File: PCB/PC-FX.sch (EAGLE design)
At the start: 11 parts, among them U1 SN74AHCT125N, U2 SN74AHCT125N

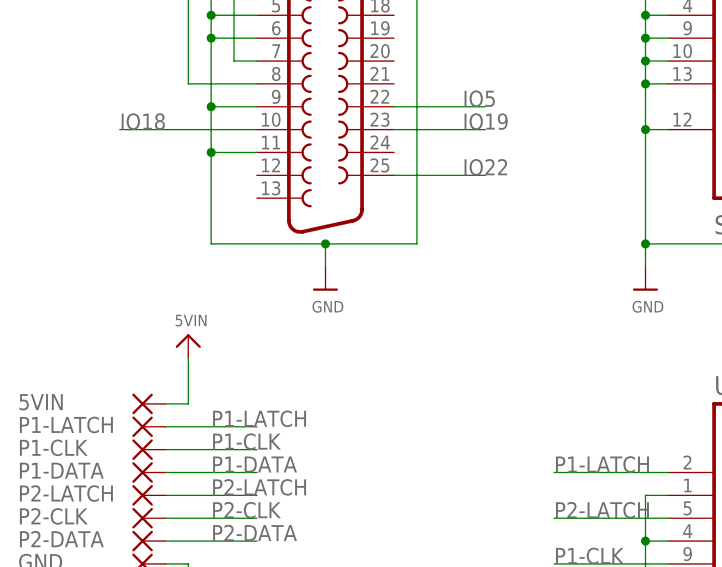
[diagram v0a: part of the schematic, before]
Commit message: Added exposed GND plane at DB25 anchors
All PCBs have been update to have exposed GND plane pads for the DB25 anchor points.

This resolves Issue 54
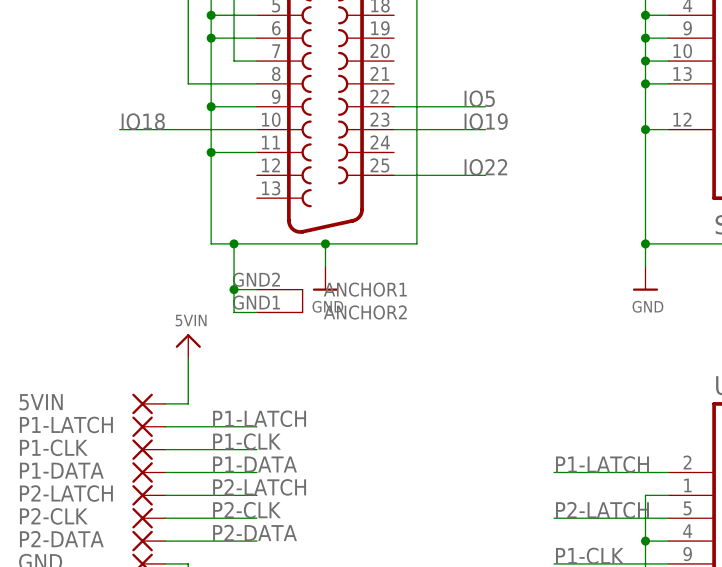
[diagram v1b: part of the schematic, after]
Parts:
- X1: device SparkFun-Retired:DB25_FEMALEH -> SparkFun-Retired:DB25_FEMALEHP
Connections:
- net GND: now also X1.ANCHOR1, X1.ANCHOR2
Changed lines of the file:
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@@
 </classes>
 <parts>
-<part name="X1" library="SparkFun-Retired" deviceset="DB25_FEMALE" device="H"/>
+<part name="X1" library="SparkFun-Retired" deviceset="DB25_FEMALE" device="HP"/>
 <part name="U$34" library="microbuilder" deviceset="VIN" device="" value="3V3IN"/>
 <part name="U$35" library="microbuilder" deviceset="VIN" device="" value="5VIN"/>
@@
 <segment>
 <wire x1="365.76" y1="-109.22" x2="355.6" y2="-109.22" width="0.1524" layer="91"/>
-<wire x1="355.6" y1="-109.22" x2="342.9" y2="-109.22" width="0.1524" layer="91"/>
+<wire x1="355.6" y1="-109.22" x2="345.44" y2="-109.22" width="0.1524" layer="91"/>
+<wire x1="345.44" y1="-109.22" x2="342.9" y2="-109.22" width="0.1524" layer="91"/>
 <wire x1="355.6" y1="-109.22" x2="355.6" y2="-111.76" width="0.1524" layer="91"/>
 <junction x="355.6" y="-109.22"/>
@@
 <wire x1="363.22" y1="-81.28" x2="365.76" y2="-81.28" width="0.1524" layer="91"/>
 <junction x="365.76" y="-81.28"/>
+<pinref part="X1" gate="-1" pin="ANCHOR2"/>
+<wire x1="347.98" y1="-116.84" x2="345.44" y2="-116.84" width="0.1524" layer="91"/>
+<wire x1="345.44" y1="-116.84" x2="345.44" y2="-114.3" width="0.1524" layer="91"/>
+<junction x="345.44" y="-109.22"/>
+<pinref part="X1" gate="-1" pin="ANCHOR1"/>
+<wire x1="345.44" y1="-114.3" x2="345.44" y2="-109.22" width="0.1524" layer="91"/>
+<wire x1="347.98" y1="-114.3" x2="345.44" y2="-114.3" width="0.1524" layer="91"/>
+<junction x="345.44" y="-114.3"/>
 </segment>
 <segment>
